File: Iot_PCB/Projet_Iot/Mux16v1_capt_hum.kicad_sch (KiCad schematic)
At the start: 5 parts, among them U10 74LS151

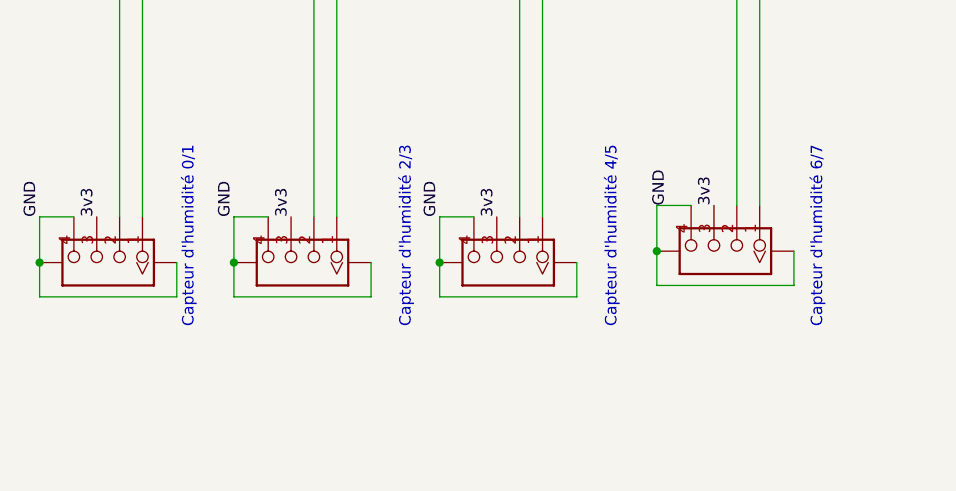
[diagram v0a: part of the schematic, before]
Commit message: remplacement des grove lora par des vrais
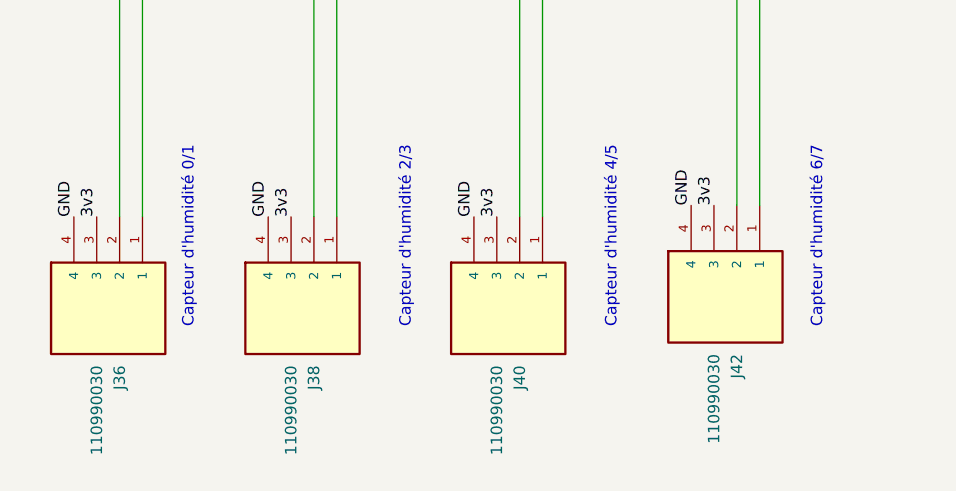
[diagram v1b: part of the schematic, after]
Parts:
- removed J32, J33, J34, J35: ~, Lora:HW4-SMD-2.0, symbol Lora-eagle-import:GROVE-CONNECTOR-SMD'DD'
- added J36, J38, J40, J42: 110990030, 110990030:SEEED_110990030, symbol grove:110990030
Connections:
- net 3v3: now also J36.3, J38.3, J40.3, J42.3
- net GND: now also J36.4, J38.4, J40.4, J42.4
- net Hum0: now also J36.1
- net Hum1: now also J36.2
- net Hum2: now also J38.2
- net Hum3: now also J38.1
- net Hum4: now also J40.2
- net Hum5: now also J40.1
- net Hum6: now also J42.2
- net Hum7: now also J42.1

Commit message: update 1-wire, pull_up i2c, switch load added but not configured yet (wait for test)
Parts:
- renumbered J36 to J37, J38 to J39, J40 to J41, J42 to J43
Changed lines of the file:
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@@
 		(dnp no)
 		(fields_autoplaced yes)
-		(property "Reference" "J42"
+		(property "Reference" "J43"
 			(at 86.3601 194.31 0)
 			(effects
@@
 		(dnp no)
 		(fields_autoplaced yes)
-		(property "Reference" "J40"
+		(property "Reference" "J41"
 			(at 62.2301 195.58 0)
 			(effects
@@
 		(dnp no)
 		(fields_autoplaced yes)
-		(property "Reference" "J36"
+		(property "Reference" "J37"
 			(at 17.7801 195.58 0)
 			(effects
@@
 		(dnp no)
 		(fields_autoplaced yes)
-		(property "Reference" "J38"
+		(property "Reference" "J39"
 			(at 39.3701 195.58 0)
 			(effects

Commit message: build(kicad): add a trace to every schematic
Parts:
- U7: renamed from U10; footprint (none) -> Package_DIP:DIP-16_W7.62mm
- renumbered J37 to J36, J39 to J38, J41 to J40, J43 to J42
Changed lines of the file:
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@@
 (kicad_sch
-	(version 20231120)
+	(version 20250114)
 	(generator "eeschema")
-	(generator_version "8.0")
+	(generator_version "9.0")
 	(paper "A4")
+	(text "Capteur d'humidité 4/5"
+		(exclude_from_sim no)
+		(at 72.39 181.356 90)
+		(effects
+			(font
+				(size 1.27 1.27)
+			)
+		)
+	)
+	(text "Capteur d'humidité 2/3"
+		(exclude_from_sim no)
+		(at 49.53 181.356 90)
+		(effects
+			(font
+				(size 1.27 1.27)
+			)
+		)
+	)
+	(text "Capteur d'humidité 6/7"
+		(exclude_from_sim no)
+		(at 95.25 181.356 90)
+		(effects
+			(font
+				(size 1.27 1.27)
+			)
+		)
+	)
+	(text "Capteur d'humidité 0/1"
+		(exclude_from_sim no)
+		(at 25.4 181.356 90)
+		(effects
+			(font
+				(size 1.27 1.27)
+			)
+		)
+	)
 	(junction
 		(at 78.74 91.44)
@@
 		)
 	)
-	(text "Capteur d'humidité 4/5"
-		(exclude_from_sim no)
-		(at 72.39 181.356 90)
-		(effects
-			(font
-				(size 1.27 1.27)
-			)
-		)
-	)
-	(text "Capteur d'humidité 2/3"
-		(exclude_from_sim no)
-		(at 49.53 181.356 90)
-		(effects
-			(font
-				(size 1.27 1.27)
-			)
-		)
-	)
-	(text "Capteur d'humidité 6/7"
-		(exclude_from_sim no)
-		(at 95.25 181.356 90)
-		(effects
-			(font
-				(size 1.27 1.27)
-			)
-		)
-	)
-	(text "Capteur d'humidité 0/1"
-		(exclude_from_sim no)
-		(at 25.4 181.356 90)
-		(effects
-			(font
-				(size 1.27 1.27)
-			)
-		)
-	)
 	(label "GND"
 		(at 34.29 179.07 90)
-		(fields_autoplaced yes)
 		(effects
 			(font
@@
 	(label "Hum7"
 		(at 88.9 139.7 0)
-		(fields_autoplaced yes)
 		(effects
 			(font
@@
 	(label "Hum0"
 		(at 38.1 104.14 270)
-		(fields_autoplaced yes)
 		(effects
 			(font
@@
 	(label "Hum4"
 		(at 48.26 104.14 270)
-		(fields_autoplaced yes)
 		(effects
 			(font
@@
 	(label "Hum1"
 		(at 17.78 140.97 180)
-		(fields_autoplaced yes)
 		(effects
 			(font
@@
 	(label "Hum5"
 		(at 50.8 104.14 270)
-		(fields_autoplaced yes)
 		(effects
 			(font
@@
 	(label "Hum6"
 		(at 86.36 138.43 180)
-		(fields_autoplaced yes)
 		(effects
 			(font
@@
 	(label "Hum4"
 		(at 62.23 139.7 180)
-		(fields_autoplaced yes)
 		(effects
 			(font
@@
 	(label "Hum5"
 		(at 64.77 139.7 0)
-		(fields_autoplaced yes)
 		(effects
 			(font
@@
 	(label "Hum7"
 		(at 55.88 104.14 270)
-		(fields_autoplaced yes)
 		(effects
 			(font
@@
 	(label "3v3"
 		(at 83.82 177.8 90)
-		(fields_autoplaced yes)
 		(effects
 			(font
@@
 	(label "Hum6"
 		(at 53.34 104.14 270)
-		(fields_autoplaced yes)
 		(effects
 			(font
@@
 	(label "3v3"
 		(at 59.69 179.07 90)
-		(fields_autoplaced yes)
 		(effects
 			(font
@@
 	(label "Hum0"
 		(at 20.32 140.97 0)
-		(fields_autoplaced yes)
 		(effects
 			(font
@@
 	(label "3v3"
 		(at 36.83 179.07 90)
-		(fields_autoplaced yes)
 		(effects
 			(font
@@
 	(label "GND"
 		(at 57.15 179.07 90)
-		(fields_autoplaced yes)
 		(effects
 			(font
@@
 	(label "Hum2"
 		(at 43.18 104.14 270)
-		(fields_autoplaced yes)
 		(effects
 			(font
@@
 	(label "Hum2"
 		(at 39.37 139.7 180)
-		(fields_autoplaced yes)
 		(effects
 			(font
@@
 	(label "GND"
 		(at 12.7 179.07 90)
-		(fields_autoplaced yes)
 		(effects
 			(font
@@
 	(label "Hum1"
 		(at 40.64 104.14 270)
-		(fields_autoplaced yes)
 		(effects
 			(font
@@
 	(label "Hum3"
 		(at 45.72 104.14 270)
-		(fields_autoplaced yes)
 		(effects
 			(font
@@
 	(label "3v3"
 		(at 15.24 179.07 90)
-		(fields_autoplaced yes)
 		(effects
 			(font
@@
 	(label "Hum3"
 		(at 41.91 139.7 0)
-		(fields_autoplaced yes)
 		(effects
 			(font
@@
 	(label "GND"
 		(at 81.28 177.8 90)
-		(fields_autoplaced yes)
 		(effects
 			(font
@@
 		(shape input)
 		(at 30.48 91.44 180)
-		(fields_autoplaced yes)
 		(effects
 			(font
@@
 		(shape input)
 		(at 66.04 104.14 270)
-		(fields_autoplaced yes)
 		(effects
 			(font
@@
 		(shape input)
 		(at 60.96 104.14 270)
-		(fields_autoplaced yes)
 		(effects
 			(font
@@
 		(shape input)
 		(at 81.28 91.44 0)
-		(fields_autoplaced yes)
 		(effects
 			(font
@@
 		(shape input)
 		(at 63.5 104.14 270)
-		(fields_autoplaced yes)
 		(effects
 			(font
@@
 		(shape input)
 		(at 38.1 78.74 90)
-		(fields_autoplaced yes)
 		(effects
 			(font
@@
 		(dnp no)
 		(fields_autoplaced yes)
-		(property "Reference" "J43"
+		(property "Reference" "J42"
 			(at 86.3601 194.31 0)
 			(effects
@@
 		(dnp no)
 		(fields_autoplaced yes)
-		(property "Reference" "J41"
+		(property "Reference" "J40"
 			(at 62.2301 195.58 0)
 			(effects
@@
 		(dnp no)
 		(fields_autoplaced yes)
-		(property "Reference" "J37"
+		(property "Reference" "J36"
 			(at 17.7801 195.58 0)
 			(effects
@@
 		(dnp no)
 		(fields_autoplaced yes)
-		(property "Reference" "U10"
+		(property "Reference" "U7"
 			(at 78.74 85.9438 90)
 			(effects
@@
 			)
 		)
-		(property "Footprint" ""
+		(property "Footprint" "Package_DIP:DIP-16_W7.62mm"
 			(at 53.34 91.44 0)
 			(effects
@@
 		(dnp no)
 		(fields_autoplaced yes)
-		(property "Reference" "J39"
+		(property "Reference" "J38"
 			(at 39.3701 195.58 0)
 			(effects

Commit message: build(kicad) : start PCB
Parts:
- J36, J38, J40, J42: footprint 110990030:SEEED_110990030 -> Grove:SEEED_110990030
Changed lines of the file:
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@@
 			)
 		)
-		(property "Footprint" "110990030:SEEED_110990030"
+		(property "Footprint" "Grove:SEEED_110990030"
 			(at 86.36 187.96 0)
 			(effects
@@
 			)
 		)
-		(property "Footprint" "110990030:SEEED_110990030"
+		(property "Footprint" "Grove:SEEED_110990030"
 			(at 62.23 189.23 0)
 			(effects
@@
 			)
 		)
-		(property "Footprint" "110990030:SEEED_110990030"
+		(property "Footprint" "Grove:SEEED_110990030"
 			(at 17.78 189.23 0)
 			(effects
@@
 			)
 		)
-		(property "Footprint" "110990030:SEEED_110990030"
+		(property "Footprint" "Grove:SEEED_110990030"
 			(at 39.37 189.23 0)
 			(effects

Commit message: pcb and schematic up to date
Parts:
- renumbered J36 to J37, J38 to J39, J40 to J41, J42 to J43, U7 to U10
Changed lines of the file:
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@@
 		(dnp no)
 		(fields_autoplaced yes)
-		(property "Reference" "J42"
+		(property "Reference" "J43"
 			(at 86.3601 194.31 0)
 			(effects
@@
 				(path "/1ed8458c-022b-42bb-9785-a8267003d72a/583ab950-f309-49b8-80a6-9ad0d562eacf"
 					(reference "J43")
-					(unit 1)
-				)
-				(path "/1ed8458c-022b-42bb-9785-a8267003d72a/67554e8a-c93b-4acb-b741-7309df9c9de1"
-					(reference "J42")
 					(unit 1)
 				)
@@
 		(dnp no)
 		(fields_autoplaced yes)
-		(property "Reference" "J40"
+		(property "Reference" "J41"
 			(at 62.2301 195.58 0)
 			(effects
@@
 				(path "/1ed8458c-022b-42bb-9785-a8267003d72a/583ab950-f309-49b8-80a6-9ad0d562eacf"
 					(reference "J41")
-					(unit 1)
-				)
-				(path "/1ed8458c-022b-42bb-9785-a8267003d72a/67554e8a-c93b-4acb-b741-7309df9c9de1"
-					(reference "J40")
 					(unit 1)
 				)
@@
 		(dnp no)
 		(fields_autoplaced yes)
-		(property "Reference" "J36"
+		(property "Reference" "J37"
 			(at 17.7801 195.58 0)
 			(effects
@@
 				(path "/1ed8458c-022b-42bb-9785-a8267003d72a/583ab950-f309-49b8-80a6-9ad0d562eacf"
 					(reference "J37")
-					(unit 1)
-				)
-				(path "/1ed8458c-022b-42bb-9785-a8267003d72a/67554e8a-c93b-4acb-b741-7309df9c9de1"
-					(reference "J36")
 					(unit 1)
 				)
@@
 		(dnp no)
 		(fields_autoplaced yes)
-		(property "Reference" "U7"
+		(property "Reference" "U10"
 			(at 78.74 85.9438 90)
 			(effects
@@
 				(path "/1ed8458c-022b-42bb-9785-a8267003d72a/583ab950-f309-49b8-80a6-9ad0d562eacf"
 					(reference "U10")
-					(unit 1)
-				)
-				(path "/1ed8458c-022b-42bb-9785-a8267003d72a/67554e8a-c93b-4acb-b741-7309df9c9de1"
-					(reference "U7")
 					(unit 1)
 				)
@@
 		(dnp no)
 		(fields_autoplaced yes)
-		(property "Reference" "J38"
+		(property "Reference" "J39"
 			(at 39.3701 195.58 0)
 			(effects
@@
 					(unit 1)
 				)
-				(path "/1ed8458c-022b-42bb-9785-a8267003d72a/67554e8a-c93b-4acb-b741-7309df9c9de1"
-					(reference "J38")
-					(unit 1)
-				)
